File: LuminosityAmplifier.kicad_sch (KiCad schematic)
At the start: 9 parts, among them J1 Lum_In, Q4 2N7000

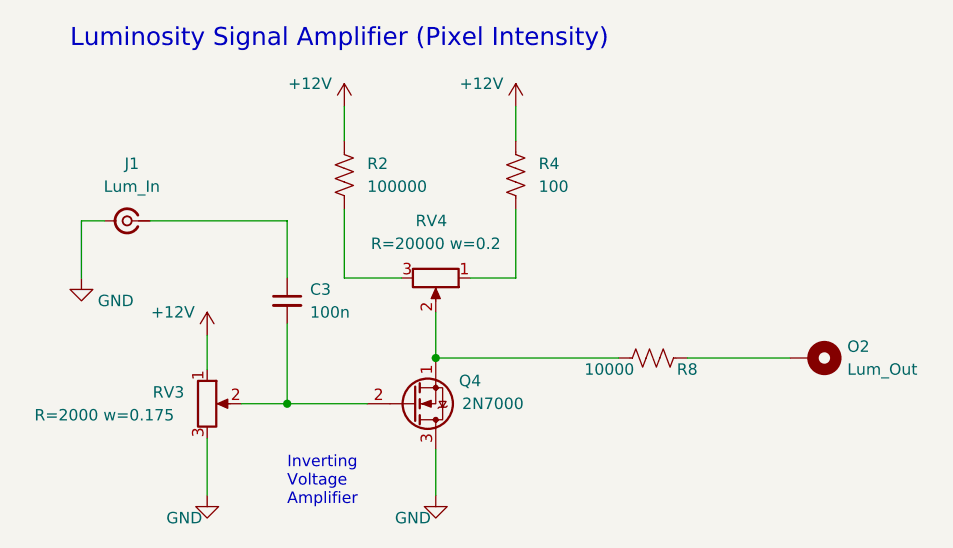
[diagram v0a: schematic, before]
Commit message: linked models so spice simulation runs
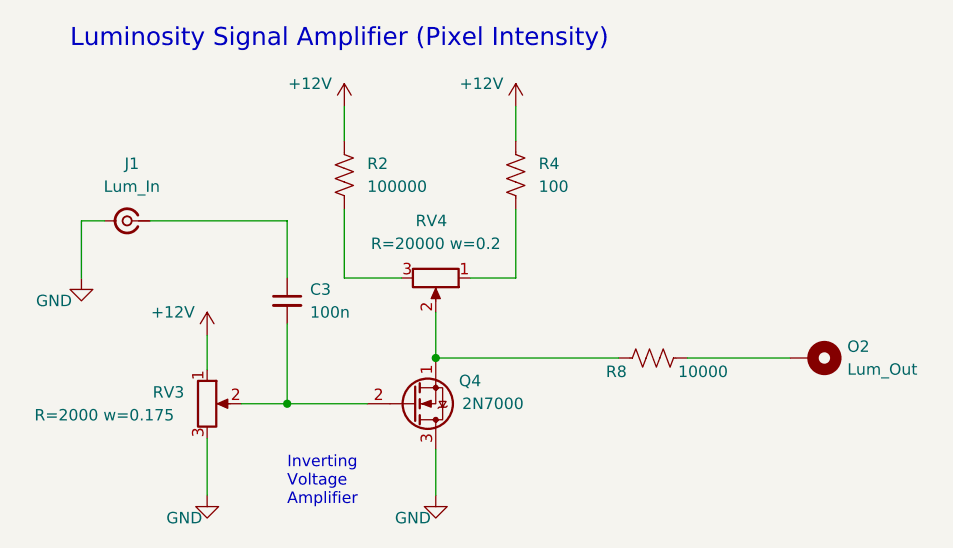
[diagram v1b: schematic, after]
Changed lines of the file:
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@@
 		(dnp no)
 		(property "Reference" "R8"
-			(at 179.07 93.98 90)
+			(at 171.196 94.234 90)
 			(effects
 				(font
@@
 		)
 		(property "Value" "10000"
-			(at 167.64 93.98 90)
+			(at 178.054 94.234 90)
 			(effects
 				(font
@@
 		)
 		(property "Value" "GND"
-			(at 115.57 86.36 0)
+			(at 108.712 86.36 0)
 			(effects
 				(font

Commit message: added new spice directives to improve simulation speed, added sections for motor drivers, micro controlers, i2c bus connections, realized that focusing coils, hv, horizontal and vertical ramp will need time stable signals (not voltage dependant like with a voltage controlled oscilator) so it will be much simpler to design them with micro controllers
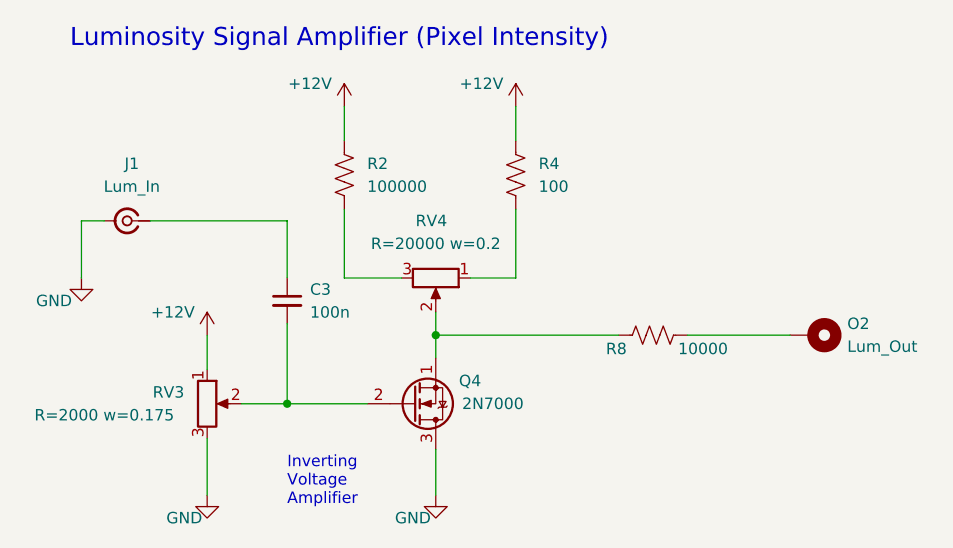
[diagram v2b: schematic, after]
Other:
- moved on the sheet: O2, R8
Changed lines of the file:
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@@
 	)
 	(junction
-		(at 151.13 92.71)
+		(at 151.13 90.17)
 		(diameter 0)
 		(color 0 0 0 0)
@@
 	(wire
 		(pts
+			(xy 151.13 90.17) (xy 151.13 92.71)
+		)
+		(stroke
+			(width 0)
+			(type default)
+		)
+	)
+	(wire
+		(pts
 			(xy 125.73 101.6) (xy 125.73 107.95)
 		)
@@
 	(wire
 		(pts
-			(xy 179.07 92.71) (xy 190.5 92.71)
+			(xy 179.07 90.17) (xy 190.5 90.17)
 		)
 		(stroke
@@
 	(wire
 		(pts
-			(xy 151.13 92.71) (xy 171.45 92.71)
-		)
-		(stroke
-			(width 0)
-			(type default)
-		)
-	)
-	(wire
-		(pts
 			(xy 134.62 97.79) (xy 143.51 97.79)
 		)
@@
 	(wire
 		(pts
-			(xy 151.13 87.63) (xy 151.13 92.71)
+			(xy 151.13 90.17) (xy 171.45 90.17)
+		)
+		(stroke
+			(width 0)
+			(type default)
+		)
+	)
+	(wire
+		(pts
+			(xy 151.13 87.63) (xy 151.13 90.17)
 		)
 		(stroke
@@
 	(symbol
 		(lib_id "Device:R_US")
-		(at 175.26 92.71 270)
+		(at 175.26 90.17 270)
 		(unit 1)
 		(exclude_from_sim no)
@@
 		(dnp no)
 		(property "Reference" "R8"
-			(at 171.196 94.234 90)
+			(at 171.196 91.694 90)
 			(effects
 				(font
@@
 		)
 		(property "Value" "10000"
-			(at 178.054 94.234 90)
+			(at 178.054 91.694 90)
 			(effects
 				(font
@@
 		)
 		(property "Footprint" "Resistor_SMD:R_0603_1608Metric"
-			(at 175.006 93.726 90)
+			(at 175.006 91.186 90)
 			(effects
 				(font
@@
 		)
 		(property "Datasheet" "~"
-			(at 175.26 92.71 0)
+			(at 175.26 90.17 0)
 			(effects
 				(font
@@
 		)
 		(property "Description" ""
-			(at 175.26 92.71 0)
+			(at 175.26 90.17 0)
 			(effects
 				(font
@@
 	(symbol
 		(lib_id "Mechanical:MountingHole_Pad")
-		(at 193.04 92.71 270)
+		(at 193.04 90.17 270)
 		(unit 1)
 		(exclude_from_sim yes)
@@
 		(fields_autoplaced yes)
 		(property "Reference" "O2"
+			(at 196.85 88.9 90)
+			(effects
+				(font
+					(size 1.27 1.27)
+				)
+				(justify left)
+			)
+		)
+		(property "Value" "Lum_Out"
 			(at 196.85 91.44 90)
 			(effects
@@
 			)
 		)
-		(property "Value" "Lum_Out"
-			(at 196.85 93.98 90)
-			(effects
-				(font
-					(size 1.27 1.27)
-				)
-				(justify left)
-			)
-		)
 		(property "Footprint" "Connector_Wire:SolderWire-0.25sqmm_1x01_D0.65mm_OD2mm_Relief"
-			(at 193.04 92.71 0)
+			(at 193.04 90.17 0)
 			(effects
 				(font
@@
 		)
 		(property "Datasheet" "~"
-			(at 193.04 92.71 0)
+			(at 193.04 90.17 0)
 			(effects
 				(font
@@
 		)
 		(property "Description" ""
-			(at 193.04 92.71 0)
+			(at 193.04 90.17 0)
 			(effects
 				(font
@@
 		)
 		(property "Sim.Device" "TLINE"
-			(at 193.04 92.71 0)
+			(at 193.04 90.17 0)
 			(effects
 				(font
@@
 		)
 		(property "Sim.Pins" "1=1+"
-			(at 193.04 92.71 0)
-			(effects
-				(font
+			(at 193.04 90.17 0)
+			(effects
+				(font
